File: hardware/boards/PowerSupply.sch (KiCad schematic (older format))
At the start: 72 parts, among them Q1 Q_NMOS_GSD, Q2 Q_NMOS_GSD, Q3 Q_NMOS_GSD, Q4 Q_NMOS_GSD, U2 ADP5050ACPZ-R7

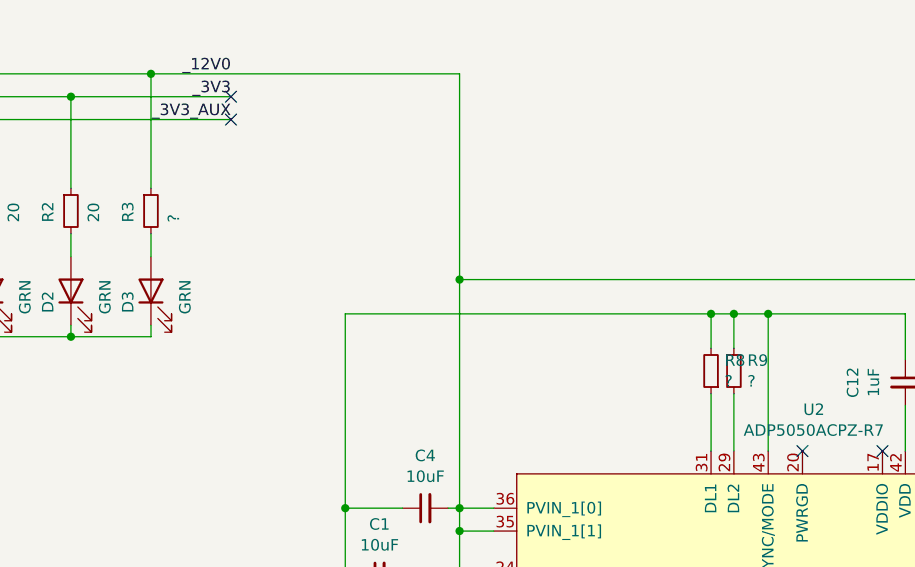
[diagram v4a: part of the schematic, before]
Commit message: Added the proper part for the +12V LED resistor
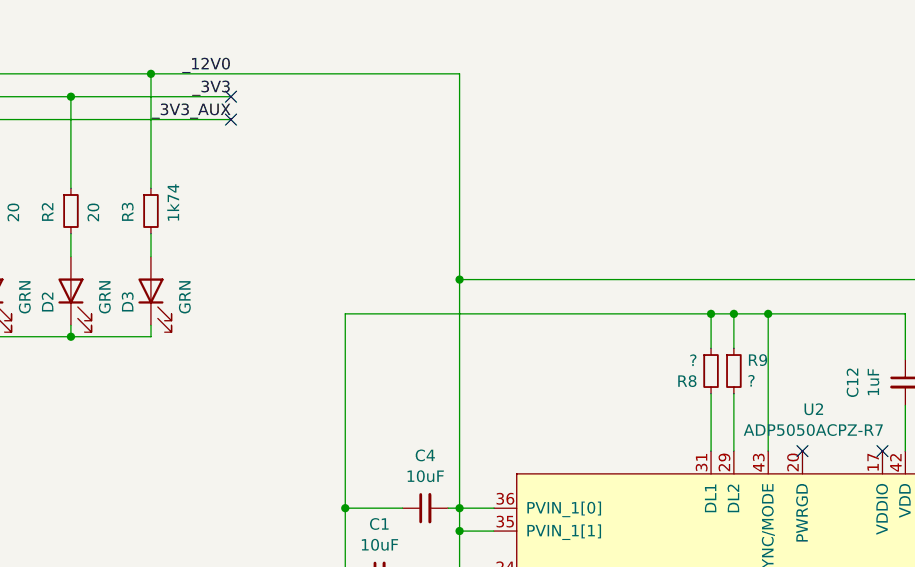
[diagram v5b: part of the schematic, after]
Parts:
- R10, R11, R12, R13, R14, R15, R16, R17, R18, R19, R20, R21, R22, R23, R24, R25, R26, R4, R5, R6, R7, R8, R9: footprint (none) -> Resistor_SMD:R_0603_1608Metric
- R3: value ? -> 1k74; footprint (none) -> Resistor_SMD:R_0603_1608Metric; MFR (none) -> Vishay Dale; MPN (none) -> CRCW06031K74FKEA
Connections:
- net GND: now also R8.1; no longer R8.2
- net at U2.31 (DL1): now also R8.2; no longer R8.1
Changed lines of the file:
@@
 P 2350 1600
 F 0 "R3" V 2250 1550 50  0000 L CNN
-F 1 "?" V 2450 1550 50  0000 L CNN
-F 2 "" H 2350 1600 50  0001 C CNN
+F 1 "1k74" V 2450 1550 50  0000 L CNN
+F 2 "Resistor_SMD:R_0603_1608Metric" H 2350 1600 50  0001 C CNN
 F 3 "~" H 2350 1600 50  0001 C CNN
+F 4 "Vishay Dale" V 2350 1600 50  0001 C CNN "MFR"
+F 5 "CRCW06031K74FKEA" V 2350 1600 50  0001 C CNN "MPN"
 	1    2350 1600
 	1    0    0    -1
@@
 F 0 "R9" H 4959 2346 50  0000 L CNN
 F 1 "?" H 4959 2255 50  0000 L CNN
-F 2 "" H 4900 2300 50  0001 C CNN
+F 2 "Resistor_SMD:R_0603_1608Metric" H 4900 2300 50  0001 C CNN
 F 3 "~" H 4900 2300 50  0001 C CNN
 	1    4900 2300
@@
 F 0 "R8" H 4741 2254 50  0000 R CNN
 F 1 "?" H 4741 2345 50  0000 R CNN
-F 2 "" H 4800 2300 50  0001 C CNN
+F 2 "Resistor_SMD:R_0603_1608Metric" H 4800 2300 50  0001 C CNN
 F 3 "~" H 4800 2300 50  0001 C CNN
 	1    4800 2300
-	-1   0    0    1
+	1    0    0    -1
 $EndComp
 $Comp
@@
 F 0 "R4" V 3454 4400 50  0000 C CNN
 F 1 "?" V 3545 4400 50  0000 C CNN
-F 2 "" H 3650 4400 50  0001 C CNN
+F 2 "Resistor_SMD:R_0603_1608Metric" H 3650 4400 50  0001 C CNN
 F 3 "~" H 3650 4400 50  0001 C CNN
 	1    3650 4400
@@
 F 0 "R17" H 6709 2946 50  0000 L CNN
 F 1 "?" H 6709 2855 50  0000 L CNN
-F 2 "" H 6650 2900 50  0001 C CNN
+F 2 "Resistor_SMD:R_0603_1608Metric" H 6650 2900 50  0001 C CNN
 F 3 "~" H 6650 2900 50  0001 C CNN
 	1    6650 2900
@@
 F 0 "R19" V 7046 3200 50  0000 C CNN
 F 1 "?" V 6955 3200 50  0000 C CNN
-F 2 "" H 6850 3200 50  0001 C CNN
+F 2 "Resistor_SMD:R_0603_1608Metric" H 6850 3200 50  0001 C CNN
 F 3 "~" H 6850 3200 50  0001 C CNN
 	1    6850 3200
@@
 F 0 "R21" H 6891 3654 50  0000 R CNN
 F 1 "?" H 6891 3745 50  0000 R CNN
-F 2 "" H 6950 3700 50  0001 C CNN
+F 2 "Resistor_SMD:R_0603_1608Metric" H 6950 3700 50  0001 C CNN
 F 3 "~" H 6950 3700 50  0001 C CNN
 	1    6950 3700
@@
 F 0 "R23" V 7346 3800 50  0000 C CNN
 F 1 "?" V 7255 3800 50  0000 C CNN
-F 2 "" H 7150 3800 50  0001 C CNN
+F 2 "Resistor_SMD:R_0603_1608Metric" H 7150 3800 50  0001 C CNN
 F 3 "~" H 7150 3800 50  0001 C CNN
 	1    7150 3800
@@
 F 0 "R25" V 7404 4000 50  0000 C CNN
 F 1 "?" V 7495 4000 50  0000 C CNN
-F 2 "" H 7600 4000 50  0001 C CNN
+F 2 "Resistor_SMD:R_0603_1608Metric" H 7600 4000 50  0001 C CNN
 F 3 "~" H 7600 4000 50  0001 C CNN
 	1    7600 4000
@@
 F 0 "R20" H 6959 4346 50  0000 L CNN
 F 1 "?" H 6959 4255 50  0000 L CNN
-F 2 "" H 6900 4300 50  0001 C CNN
+F 2 "Resistor_SMD:R_0603_1608Metric" H 6900 4300 50  0001 C CNN
 F 3 "~" H 6900 4300 50  0001 C CNN
 	1    6900 4300
@@
 F 0 "R18" H 6759 4196 50  0000 L CNN
 F 1 "?" H 6759 4105 50  0000 L CNN
-F 2 "" H 6700 4150 50  0001 C CNN
+F 2 "Resistor_SMD:R_0603_1608Metric" H 6700 4150 50  0001 C CNN
 F 3 "~" H 6700 4150 50  0001 C CNN
 	1    6700 4150
@@
 F 0 "R26" V 7404 5050 50  0000 C CNN
 F 1 "?" V 7495 5050 50  0000 C CNN
-F 2 "" H 7600 5050 50  0001 C CNN
+F 2 "Resistor_SMD:R_0603_1608Metric" H 7600 5050 50  0001 C CNN
 F 3 "~" H 7600 5050 50  0001 C CNN
 	1    7600 5050
@@
 F 0 "R22" H 6891 4754 50  0000 R CNN
 F 1 "?" H 6891 4845 50  0000 R CNN
-F 2 "" H 6950 4800 50  0001 C CNN
+F 2 "Resistor_SMD:R_0603_1608Metric" H 6950 4800 50  0001 C CNN
 F 3 "~" H 6950 4800 50  0001 C CNN
 	1    6950 4800
@@
 F 0 "R24" H 7141 4854 50  0000 R CNN
 F 1 "?" H 7141 4945 50  0000 R CNN
-F 2 "" H 7200 4900 50  0001 C CNN
+F 2 "Resistor_SMD:R_0603_1608Metric" H 7200 4900 50  0001 C CNN
 F 3 "~" H 7200 4900 50  0001 C CNN
 	1    7200 4900
@@
 F 0 "R16" V 6054 5600 50  0000 C CNN
 F 1 "?" V 6145 5600 50  0000 C CNN
-F 2 "" H 6250 5600 50  0001 C CNN
+F 2 "Resistor_SMD:R_0603_1608Metric" H 6250 5600 50  0001 C CNN
 F 3 "~" H 6250 5600 50  0001 C CNN
 	1    6250 5600
@@
 F 0 "R15" V 5854 5750 50  0000 C CNN
 F 1 "?" V 5945 5750 50  0000 C CNN
-F 2 "" H 6050 5750 50  0001 C CNN
+F 2 "Resistor_SMD:R_0603_1608Metric" H 6050 5750 50  0001 C CNN
 F 3 "~" H 6050 5750 50  0001 C CNN
 	1    6050 5750
@@
 F 0 "R14" H 5591 5704 50  0000 R CNN
 F 1 "?" H 5591 5795 50  0000 R CNN
-F 2 "" H 5650 5750 50  0001 C CNN
+F 2 "Resistor_SMD:R_0603_1608Metric" H 5650 5750 50  0001 C CNN
 F 3 "~" H 5650 5750 50  0001 C CNN
 	1    5650 5750
@@
 F 0 "R13" H 5609 5796 50  0000 L CNN
 F 1 "?" H 5609 5705 50  0000 L CNN
-F 2 "" H 5550 5750 50  0001 C CNN
+F 2 "Resistor_SMD:R_0603_1608Metric" H 5550 5750 50  0001 C CNN
 F 3 "~" H 5550 5750 50  0001 C CNN
 	1    5550 5750
@@
 F 0 "R12" V 5204 6500 50  0000 C CNN
 F 1 "?" V 5295 6500 50  0000 C CNN
-F 2 "" H 5400 6500 50  0001 C CNN
+F 2 "Resistor_SMD:R_0603_1608Metric" H 5400 6500 50  0001 C CNN
 F 3 "~" H 5400 6500 50  0001 C CNN
 	1    5400 6500
@@
 F 0 "R11" V 5054 6000 50  0000 C CNN
 F 1 "?" V 5145 6000 50  0000 C CNN
-F 2 "" H 5250 6000 50  0001 C CNN
+F 2 "Resistor_SMD:R_0603_1608Metric" H 5250 6000 50  0001 C CNN
 F 3 "~" H 5250 6000 50  0001 C CNN
 	1    5250 6000
@@
 F 0 "R10" V 4904 6200 50  0000 C CNN
 F 1 "?" V 4995 6200 50  0000 C CNN
-F 2 "" H 5100 6200 50  0001 C CNN
+F 2 "Resistor_SMD:R_0603_1608Metric" H 5100 6200 50  0001 C CNN
 F 3 "~" H 5100 6200 50  0001 C CNN
 	1    5100 6200
@@
 F 0 "R7" H 4641 5704 50  0000 R CNN
 F 1 "?" H 4641 5795 50  0000 R CNN
-F 2 "" H 4700 5750 50  0001 C CNN
+F 2 "Resistor_SMD:R_0603_1608Metric" H 4700 5750 50  0001 C CNN
 F 3 "~" H 4700 5750 50  0001 C CNN
 	1    4700 5750
@@
 F 0 "R6" V 4404 5750 50  0000 C CNN
 F 1 "?" V 4495 5750 50  0000 C CNN
-F 2 "" H 4600 5750 50  0001 C CNN
+F 2 "Resistor_SMD:R_0603_1608Metric" H 4600 5750 50  0001 C CNN
 F 3 "~" H 4600 5750 50  0001 C CNN
 	1    4600 5750
@@
 F 0 "R5" V 4254 6500 50  0000 C CNN
 F 1 "?" V 4345 6500 50  0000 C CNN
-F 2 "" H 4450 6500 50  0001 C CNN
+F 2 "Resistor_SMD:R_0603_1608Metric" H 4450 6500 50  0001 C CNN
 F 3 "~" H 4450 6500 50  0001 C CNN
 	1    4450 6500

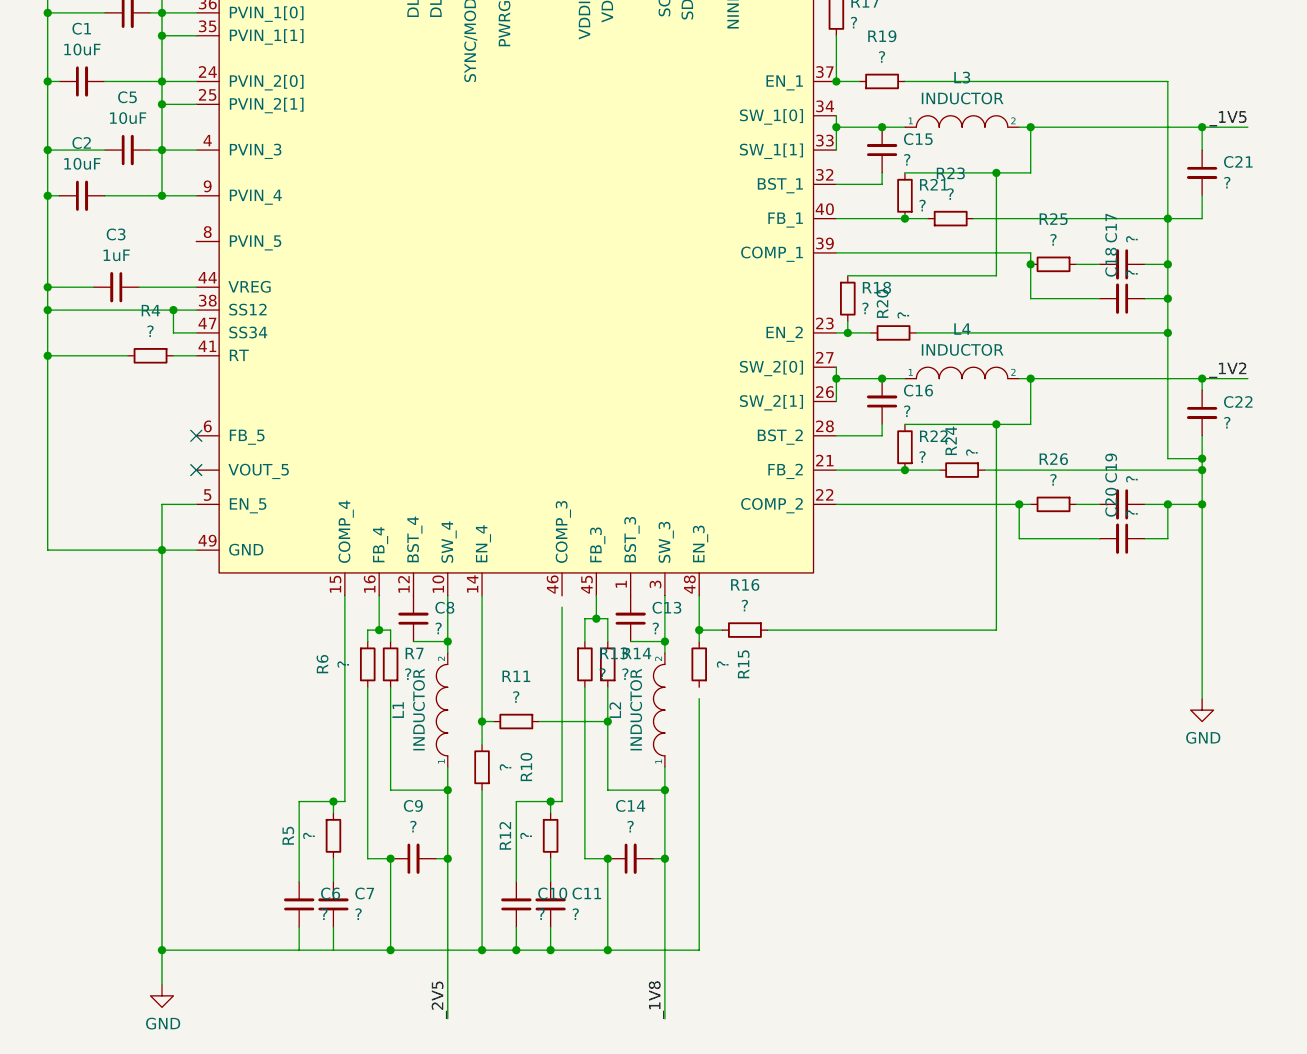
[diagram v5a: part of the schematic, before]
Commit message: flipped ome parts to clean up how the lables were placed
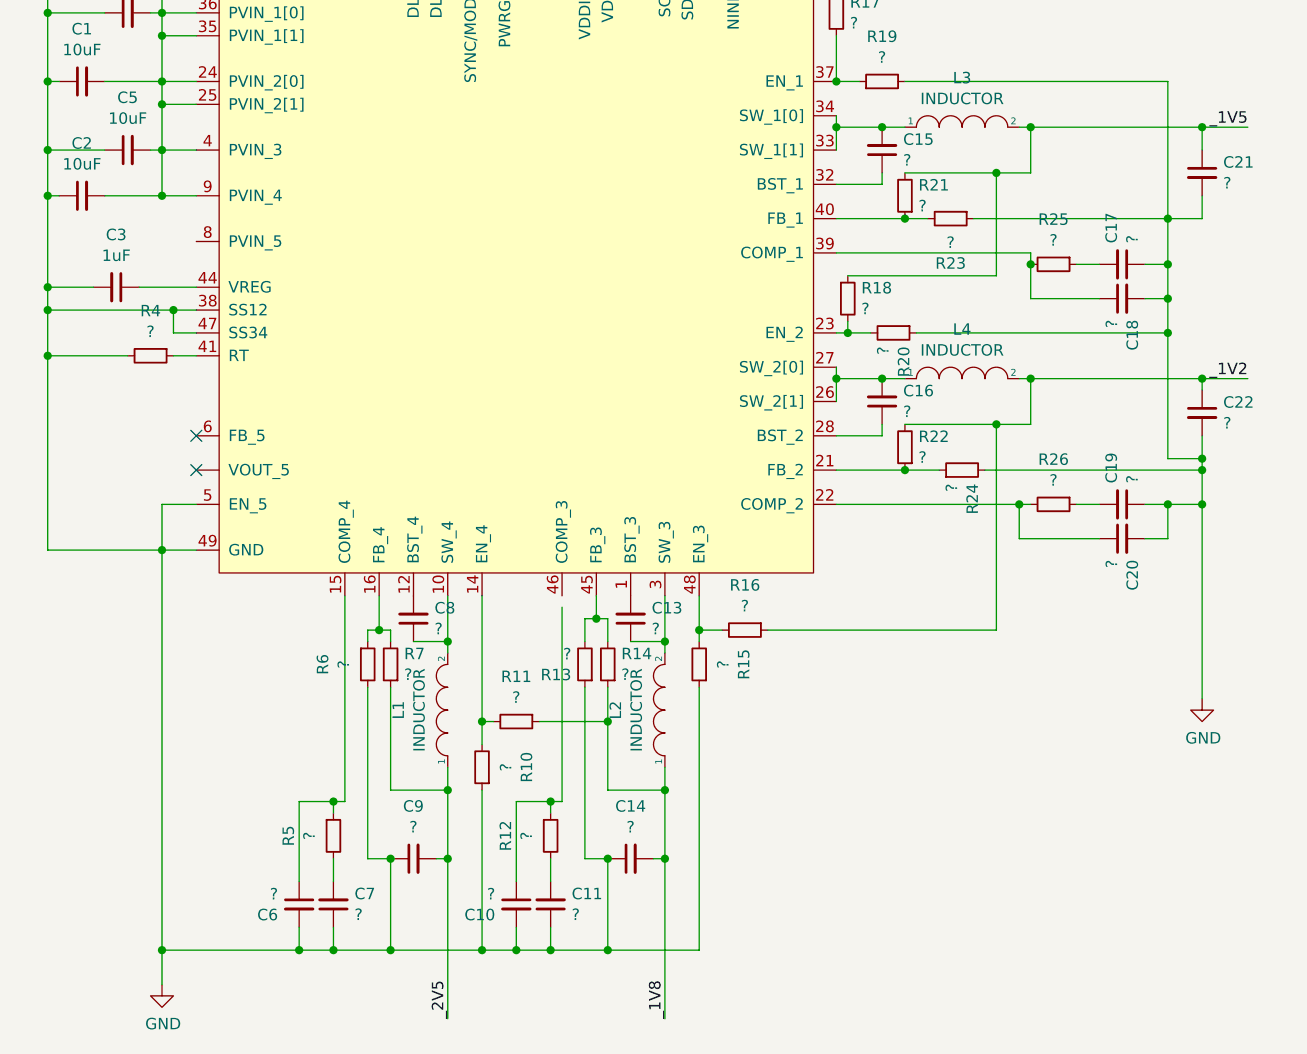
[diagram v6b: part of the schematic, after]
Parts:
- D5: value GRN -> GRN
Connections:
- net GND: now also C10.2, C18.2, C20.2, C6.2, C7.1, R13.1, R15.1, R20.1, R23.1, R24.2; no longer C10.1, C18.1, C20.1, R13.2, R20.2, R23.2, R24.1
- net at R5.1, U2.15 (COMP_4): now also C6.1; no longer C6.2
- net at R22.1, U2.21 (FB_2): now also R24.1; no longer R24.2
- net at R26.2, U2.22 (COMP_2): now also C20.1; no longer C20.2
- net at R18.2, U2.23 (EN_2): now also R20.2; no longer R20.1
- net at R25.2, U2.39 (COMP_1): now also C18.1; no longer C18.2
- net at R21.1, U2.40 (FB_1): now also R23.2; no longer R23.1
- net at R14.2, U2.45 (FB_3): now also R13.2; no longer R13.1
- net at R12.1: now also C10.1; no longer C10.2
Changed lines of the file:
@@
 	5900 6600 5850 6600
 Wire Wire Line
-	3700 7000 4700 7000
+	3700 7000 4300 7000
 Wire Wire Line
 	4700 7000 4700 6600
@@
 F 3 "~" H 7150 3800 50  0001 C CNN
 	1    7150 3800
-	0    -1   -1   0
+	0    1    1    0
 $EndComp
 Wire Wire Line
@@
 F 5 "" V 7900 4150 50  0001 C CNN "MPN"
 	1    7900 4150
-	0    1    1    0
+	0    -1   -1   0
 $EndComp
 $Comp
@@
 F 3 "~" H 6900 4300 50  0001 C CNN
 	1    6900 4300
-	0    -1   -1   0
+	0    1    1    0
 $EndComp
 $Comp
@@
 F 5 "" V 7900 5200 50  0001 C CNN "MPN"
 	1    7900 5200
-	0    1    1    0
+	0    -1   -1   0
 $EndComp
 $Comp
@@
 F 3 "~" H 7200 4900 50  0001 C CNN
 	1    7200 4900
-	0    1    1    0
+	0    -1   -1   0
 $EndComp
 Wire Wire Line
@@
 	7350 4700 7500 4700
 Wire Wire Line
-	6050 5900 6050 7000
+	6050 5850 6050 7000
 Wire Wire Line
 	6050 7000 5650 7000
@@
 F 3 "~" H 5550 5750 50  0001 C CNN
 	1    5550 5750
-	1    0    0    -1
+	-1   0    0    1
 $EndComp
 Wire Wire Line
@@
 F 5 "" V 5250 6800 50  0001 C CNN "MPN"
 	1    5250 6800
-	-1   0    0    1
+	1    0    0    -1
 $EndComp
 Wire Wire Line
@@
 F 5 "" V 4300 6800 50  0001 C CNN "MPN"
 	1    4300 6800
-	-1   0    0    1
+	1    0    0    -1
 $EndComp
 Wire Wire Line
@@
 Wire Wire Line
 	4450 6350 4450 6400
-Wire Wire Line
-	4450 6900 4450 7000
-Wire Wire Line
-	4300 6900 4300 7000
 Wire Wire Line
 	4300 6350 4450 6350
@@
 F 5 "150060GS75000" H 10700 2000 50  0001 C CNN "MPN"
 	1    10700 2000
-	1    0    0    -1
-$EndComp
-$Comp
-L Device:LED D5
-U 1 1 5EFFCB3F
-P 10700 1550
-F 0 "D5" H 10700 1650 50  0000 R CNN
-F 1 "GRN" H 10750 1400 50  0000 R CNN
-F 2 "LED_SMD:LED_0603_1608Metric" H 10700 1550 50  0001 C CNN
-F 3 "~" H 10700 1550 50  0001 C CNN
-F 4 "Würth Elektronik" H 10700 1550 50  0001 C CNN "MFR"
-F 5 "150060GS75000" H 10700 1550 50  0001 C CNN "MPN"
-	1    10700 1550
 	1    0    0    -1
 $EndComp
@@
 	1    0    0    -1
 $EndComp
+Wire Wire Line
+	4450 6900 4450 7000
+Connection ~ 4450 7000
+Wire Wire Line
+	4450 7000 4700 7000
+Wire Wire Line
+	4300 6900 4300 7000
+Connection ~ 4300 7000
+Wire Wire Line
+	4300 7000 4450 7000
+$Comp
+L Device:LED D5
+U 1 1 5EFFCB3F
+P 10700 1550
+F 0 "D5" H 10700 1650 50  0000 R CNN
+F 1 "GRN " H 10750 1400 50  0000 R CNN
+F 2 "LED_SMD:LED_0603_1608Metric" H 10700 1550 50  0001 C CNN
+F 3 "~" H 10700 1550 50  0001 C CNN
+F 4 "Würth Elektronik" H 10700 1550 50  0001 C CNN "MFR"
+F 5 "150060GS75000" H 10700 1550 50  0001 C CNN "MPN"
+	1    10700 1550
+	1    0    0    -1
+$EndComp
